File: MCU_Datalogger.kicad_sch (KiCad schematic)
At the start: 0 parts

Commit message: Have added required symbols to the schematic sheets
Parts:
- added BAT1: BS-7, digikey-footprints:Battery_Holder_Coin_2032_BS-7, symbol dk_Battery-Holders-Clips-Contacts:BS-7
- added C1, C2, C3, C4: C, symbol Device:C
- added C5: C_Polarized, symbol Device:C_Polarized
- added D1, D2: LED, symbol Device:LED
- added H1, H2, H3, H4: MountingHole, symbol Mechanical:MountingHole
- added R1, R2, R3, R4, R5, R6, R7: R, symbol Device:R
- added U1, U2: 24LC1025, symbol Memory_EEPROM:24LC1025
- added U3: DS1337S_, DS1337S_:SOIC127P600X175-8N, symbol DS1337S_:DS1337S_
- added U4: ATMEGA328P-AU, ATMEGA328P-AU:QFP80P900X900X120-32N, symbol ATMEGA328P-AU:ATMEGA328P-AU
- added Y1, Y2: Crystal, symbol Device:Crystal
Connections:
- new net: U4.21 (GND), U4.3 (GND), U4.5 (GND)
- new net: U4.4 (VCC), U4.6 (VCC)
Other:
- added sheet Connectors (connectors.kicad_sch)
- title: (none) -> ${project_name}

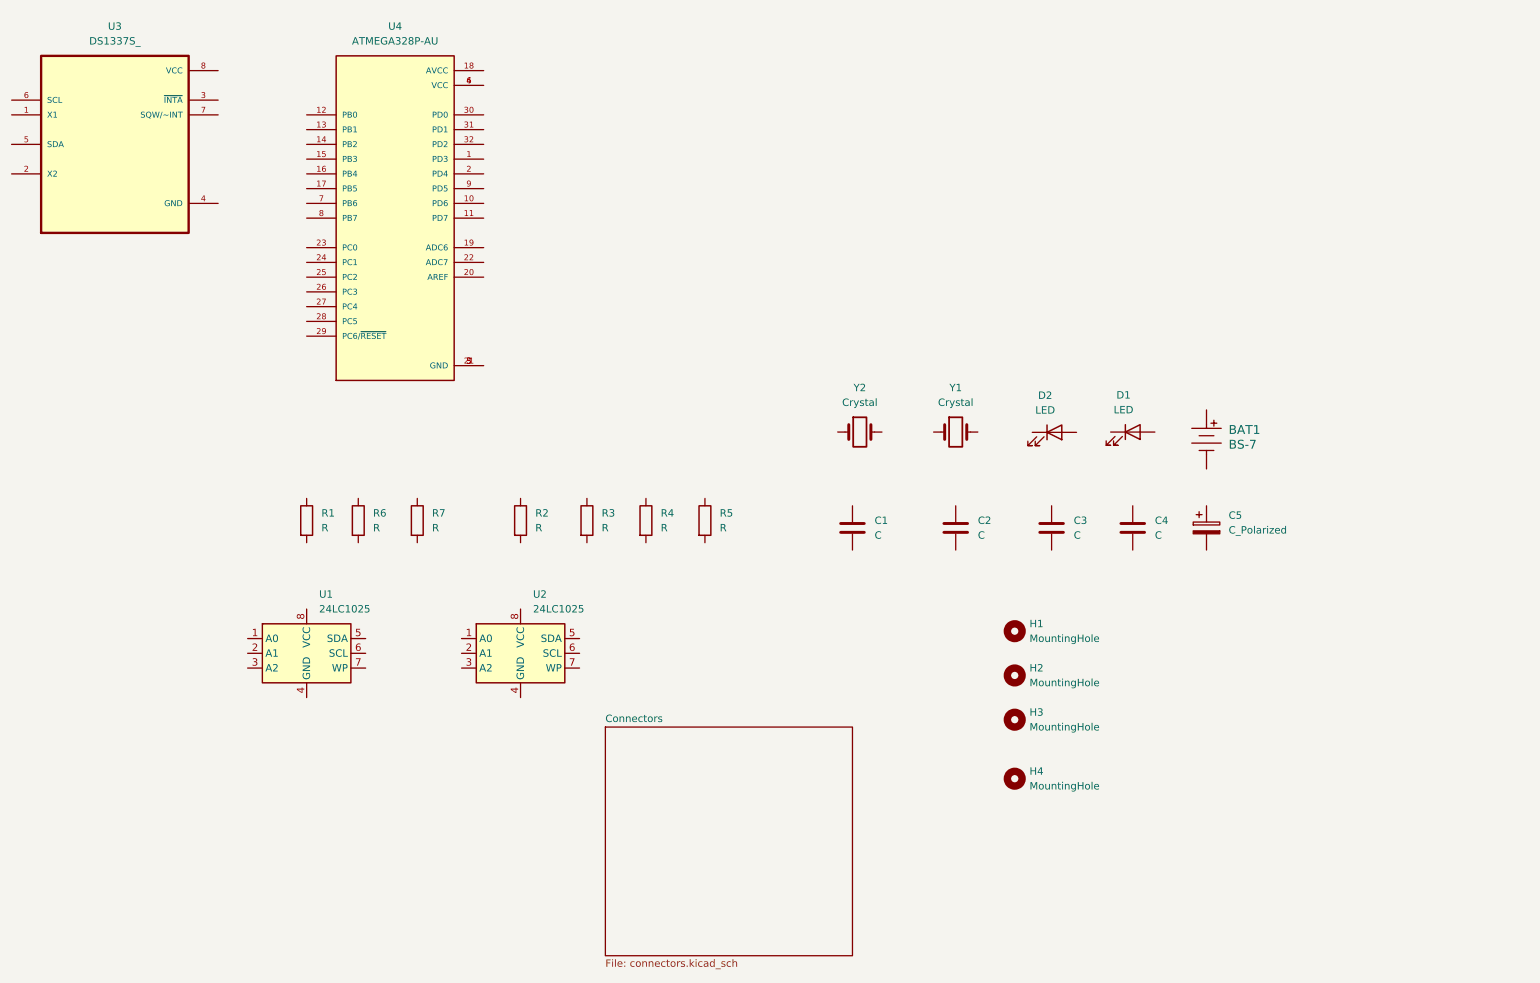
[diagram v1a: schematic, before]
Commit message: Changed locations of symbols(arrange).
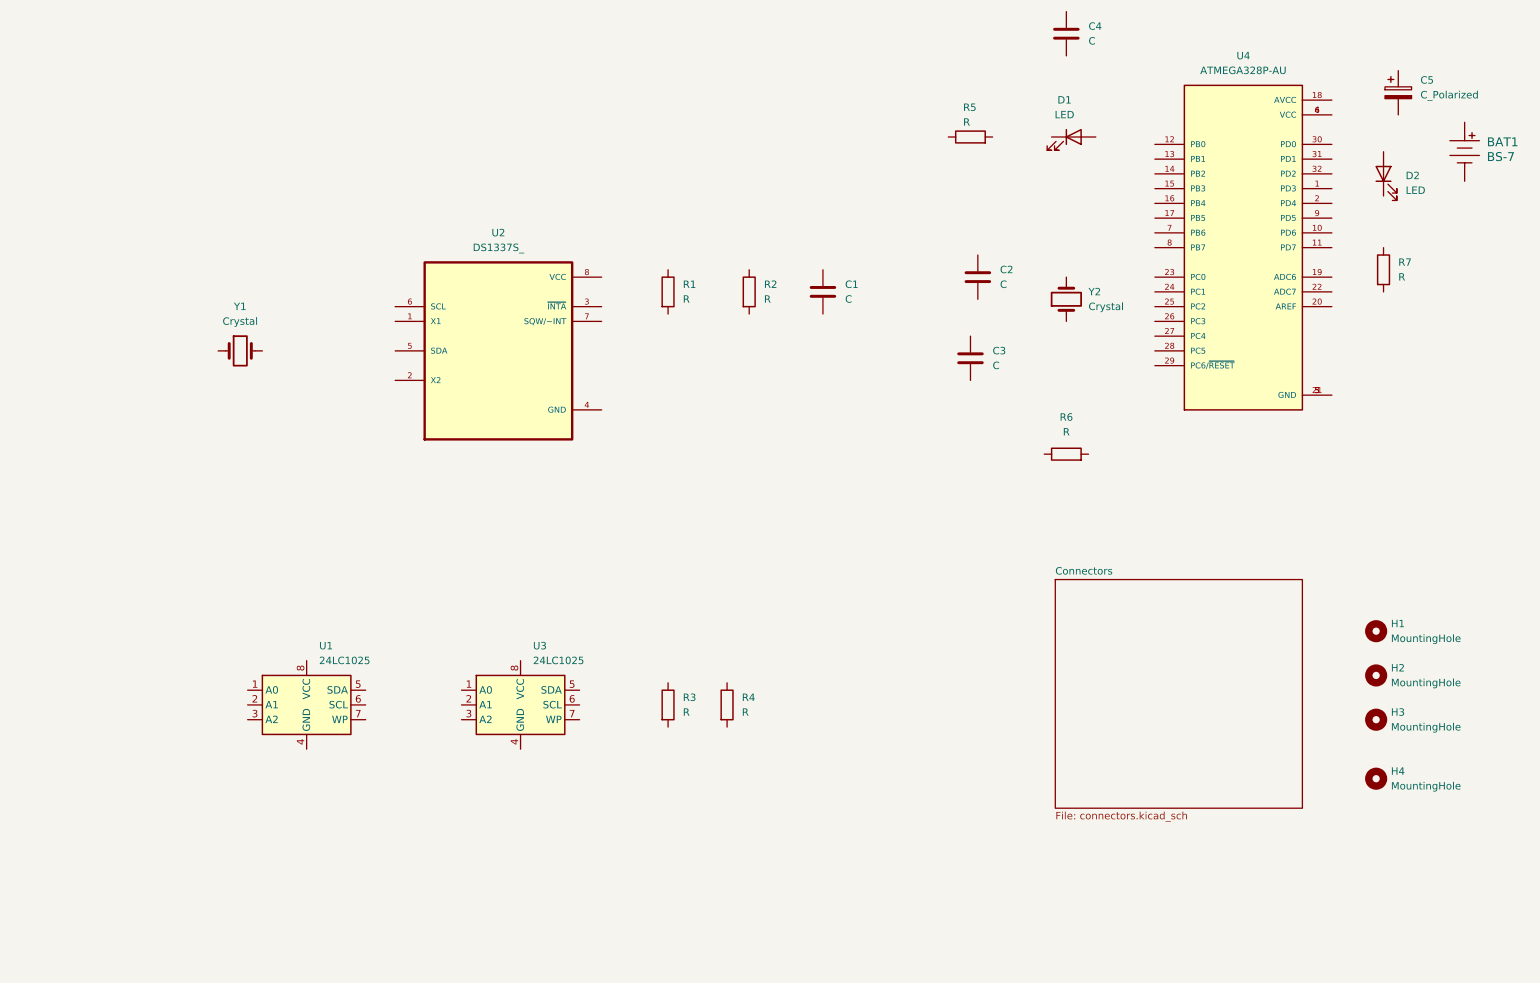
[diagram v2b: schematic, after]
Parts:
- renumbered C4 to C1, C1 to C4, D2 to D1, D1 to D2, R4 to R1, R3 to R2, R6 to R3, R7 to R4, R1 to R6, R2 to R7, U3 to U2, U2 to U3, Y2 to Y1, Y1 to Y2
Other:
- moved on the sheet: BAT1, C1, C2, C3, C4, C5, D1, D2, H1, H2, H3, H4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

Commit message: Added component values
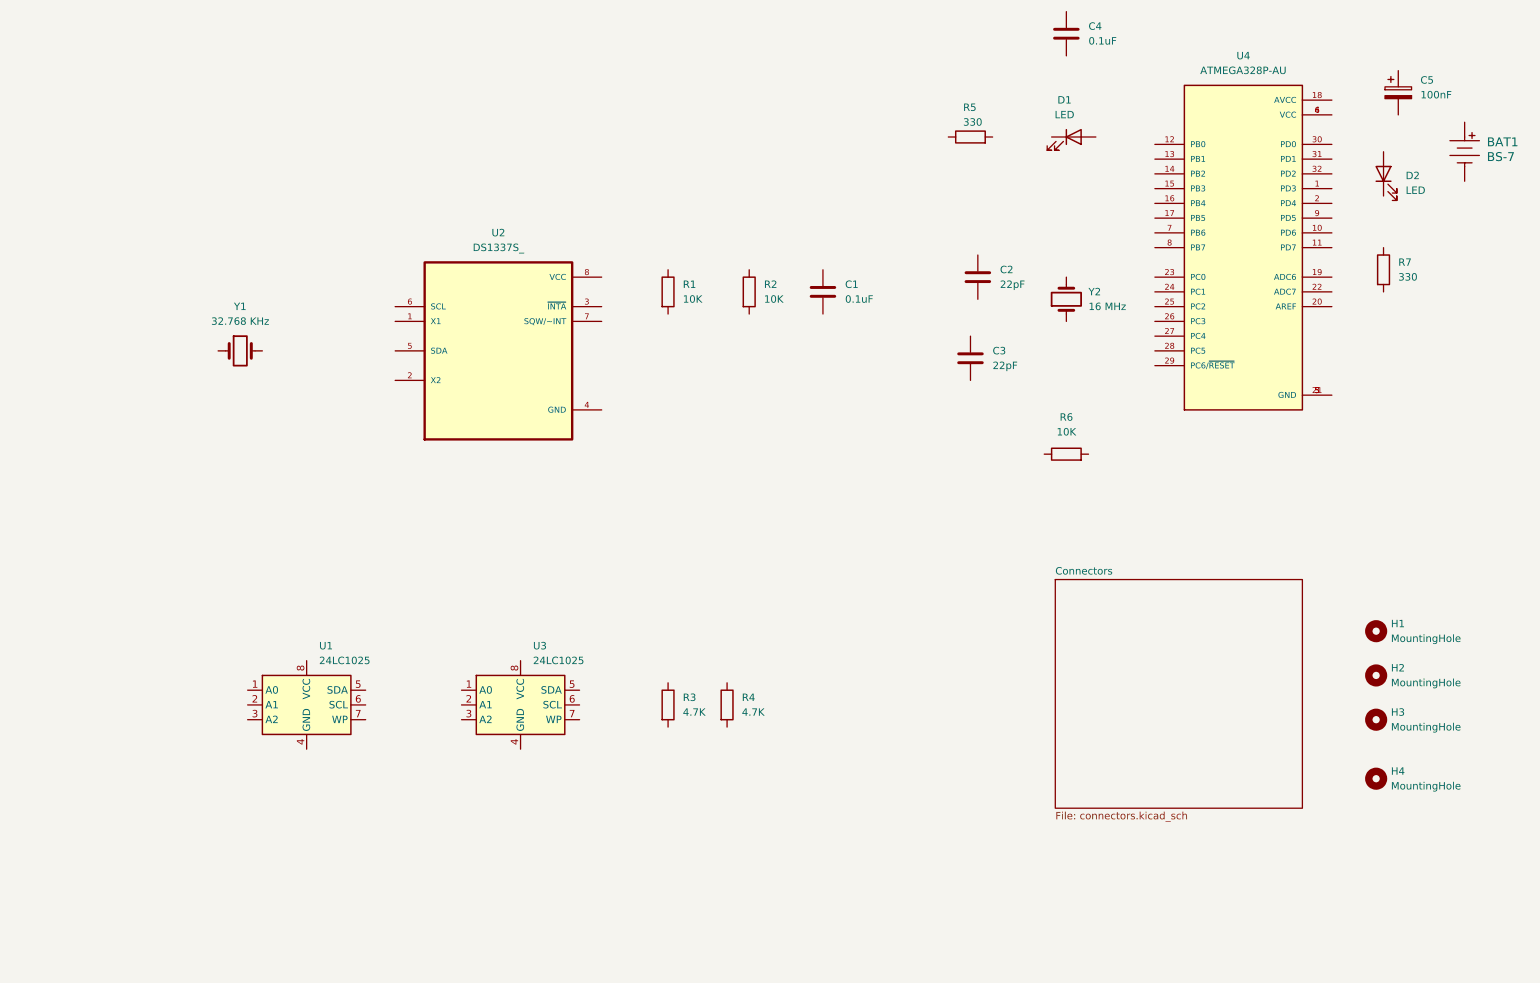
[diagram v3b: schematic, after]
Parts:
- C1, C4: value C -> 0.1uF
- C2, C3: value C -> 22pF
- C5: value C_Polarized -> 100nF
- R1, R2, R6: value R -> 10K
- R3, R4: value R -> 4.7K
- R5, R7: value R -> 330
- Y1: value Crystal -> 32.768 KHz
- Y2: value Crystal -> 16 MHz
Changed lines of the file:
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@@
 			)
 		)
-		(property "Value" "R"
+		(property "Value" "10K"
 			(at 208.28 96.52 90)
 			(effects
@@
 			)
 		)
-		(property "Value" "R"
+		(property "Value" "10K"
 			(at 142.24 73.6599 0)
 			(effects
@@
 			)
 		)
-		(property "Value" "C"
+		(property "Value" "0.1uF"
 			(at 170.18 73.6599 0)
 			(effects
@@
 			)
 		)
+		(property "Purpose" ""
+			(at 166.37 72.39 0)
+			(effects
+				(font
+					(size 1.27 1.27)
+				)
+			)
+		)
 		(pin "1"
 		)
@@
 			)
 		)
-		(property "Value" "Crystal"
+		(property "Value" "32.768 KHz"
 			(at 66.04 77.47 0)
 			(effects
@@
 			)
 		)
+		(property "Purpose" ""
+			(at 66.04 82.55 0)
+			(effects
+				(font
+					(size 1.27 1.27)
+				)
+			)
+		)
 		(pin "1"
 		)
@@
 			)
 		)
-		(property "Value" "C"
+		(property "Value" "22pF"
 			(at 196.85 71.1199 0)
 			(effects
@@
 			)
 		)
-		(property "Value" "Crystal"
+		(property "Value" "16 MHz"
 			(at 212.09 74.9299 90)
 			(effects
@@
 			)
 		)
-		(property "Value" "R"
+		(property "Value" "4.7K"
 			(at 152.4 144.7799 0)
 			(effects
@@
 			)
 		)
-		(property "Value" "R"
+		(property "Value" "330"
 			(at 190.5 43.1799 90)
 			(effects
@@
 			)
 		)
-		(property "Value" "R"
+		(property "Value" "10K"
 			(at 156.21 73.6599 0)
 			(effects
@@
 			)
 		)
-		(property "Value" "C_Polarized"
+		(property "Value" "100nF"
 			(at 269.24 38.4809 0)
 			(effects
@@
 			)
 		)
-		(property "Value" "C"
+		(property "Value" "0.1uF"
 			(at 212.09 29.2099 0)
 			(effects
@@
 			)
 		)
-		(property "Value" "R"
+		(property "Value" "330"
 			(at 265.43 69.8499 0)
 			(effects
@@
 			)
 		)
-		(property "Value" "R"
+		(property "Value" "4.7K"
 			(at 142.24 144.7799 0)
 			(effects
@@
 			)
 		)
-		(property "Value" "C"
+		(property "Value" "22pF"
 			(at 195.58 85.0899 0)
 			(effects
